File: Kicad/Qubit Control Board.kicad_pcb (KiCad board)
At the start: 6 copper layers, 144 x 81.5 mm, 147 parts, among them J1 USB_C_Receptacle_PowerOnly_6P, J2 CLK_Pins, J3 Idata, J4 Qdata, J5 SPIdata, J6 SMA, U1 LT3045xMSE, U2 TRF372017IRGZR, U3 LT3045xMSE, U4 LT3045xMSE, U5 SN65LVDS1DBV, U6 AD9743BCPZ, Y1 SiT8008xx-3x-xxN, Y2 CVHD-950-100.000

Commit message: board resizing
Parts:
- moved U2 74.1 mm to (155.8, 72.8)
- moved Y2 9.86 mm to (81.7, 30.1)
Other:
- board size 144 x 81.5 mm -> 64 x 81.5 mm

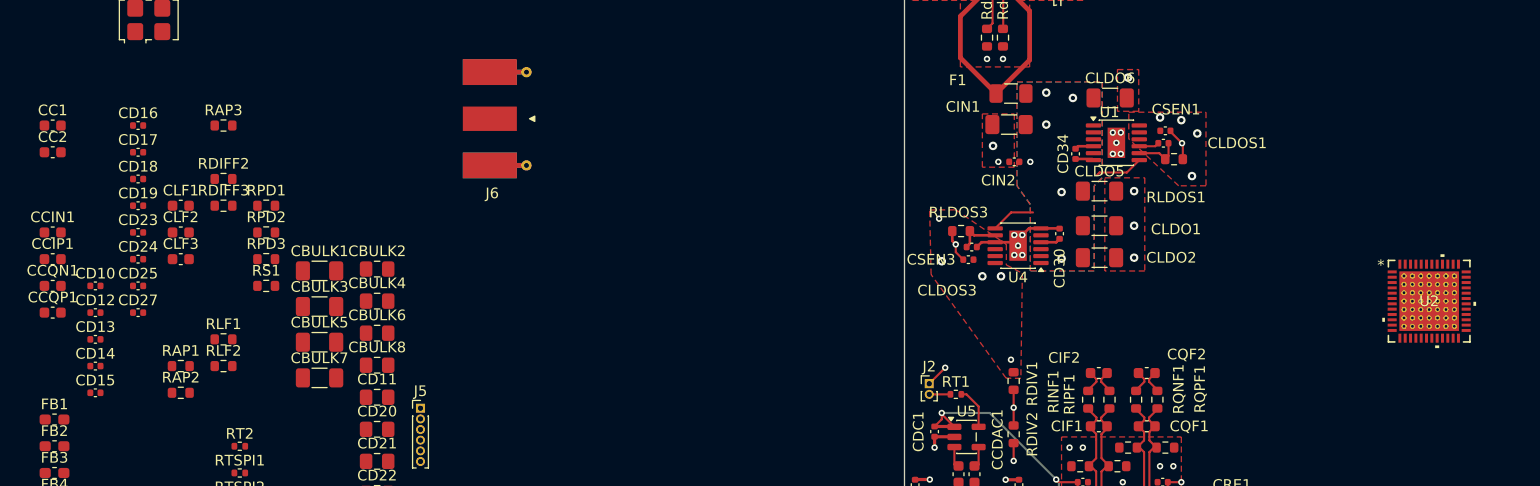
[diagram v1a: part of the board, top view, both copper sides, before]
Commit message: Added bulk caps to 3.3 and 1.8 (routing)
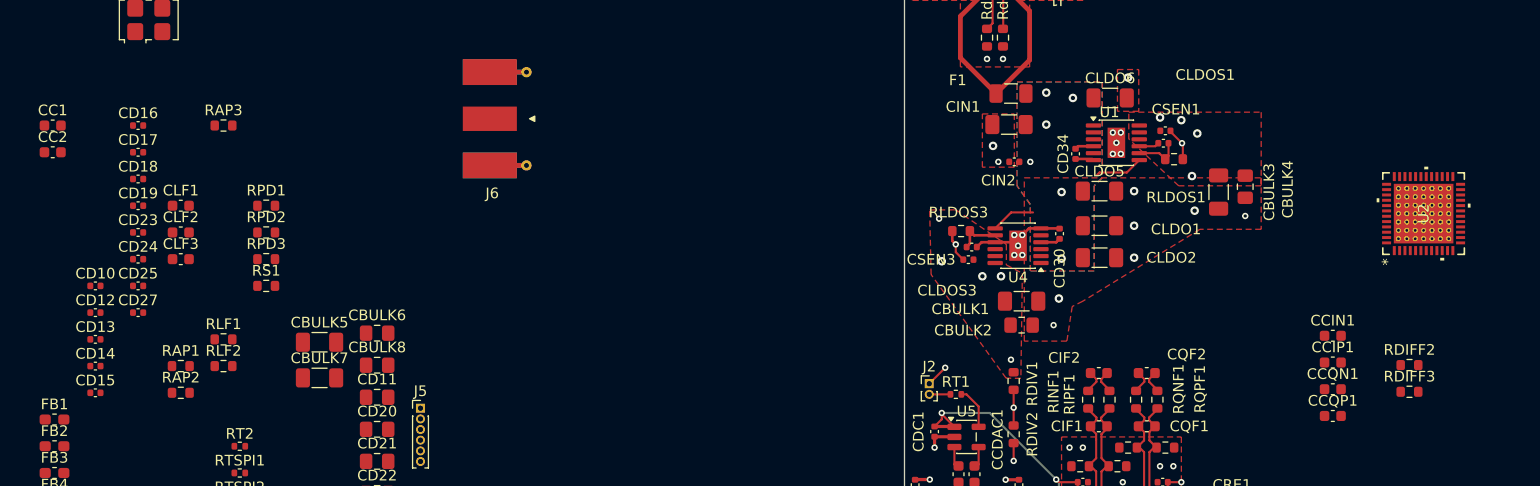
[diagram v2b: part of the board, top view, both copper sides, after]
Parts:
- moved CCIN1 120.6 mm to (146.7, 76.0)
- moved CCIP1 120.6 mm to (146.7, 78.5)
- moved CCQN1 120.6 mm to (146.7, 81.0)
- moved CCQP1 120.6 mm to (146.7, 83.5)
- moved RDIFF2 112.7 mm to (153.9, 78.8)
- moved RDIFF3 112.7 mm to (153.9, 81.3)
- moved CBULK3 85.1 mm to (136.0, 62.5), turned to -90 degrees
- moved CBULK4 82.2 mm to (138.5, 62.0), turned to -90 degrees
- moved CBULK1 66.0 mm to (117.5, 72.8)
- moved CBULK2 60.8 mm to (117.5, 75.0)
- moved U2 8.24 mm to (155.2, 64.5), turned to 90 degrees
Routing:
- net GND: vias 55 -> 59

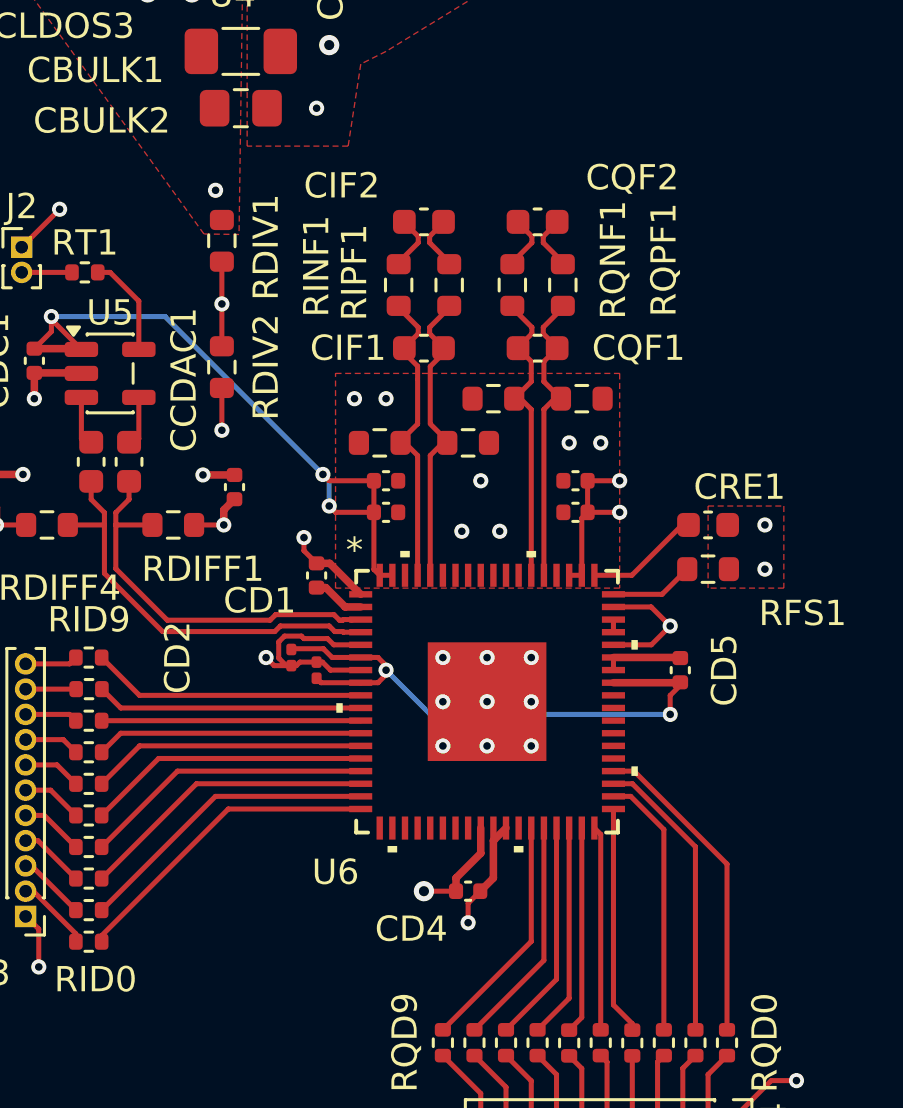
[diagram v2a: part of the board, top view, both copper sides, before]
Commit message: moved decoupling caps to the bottom
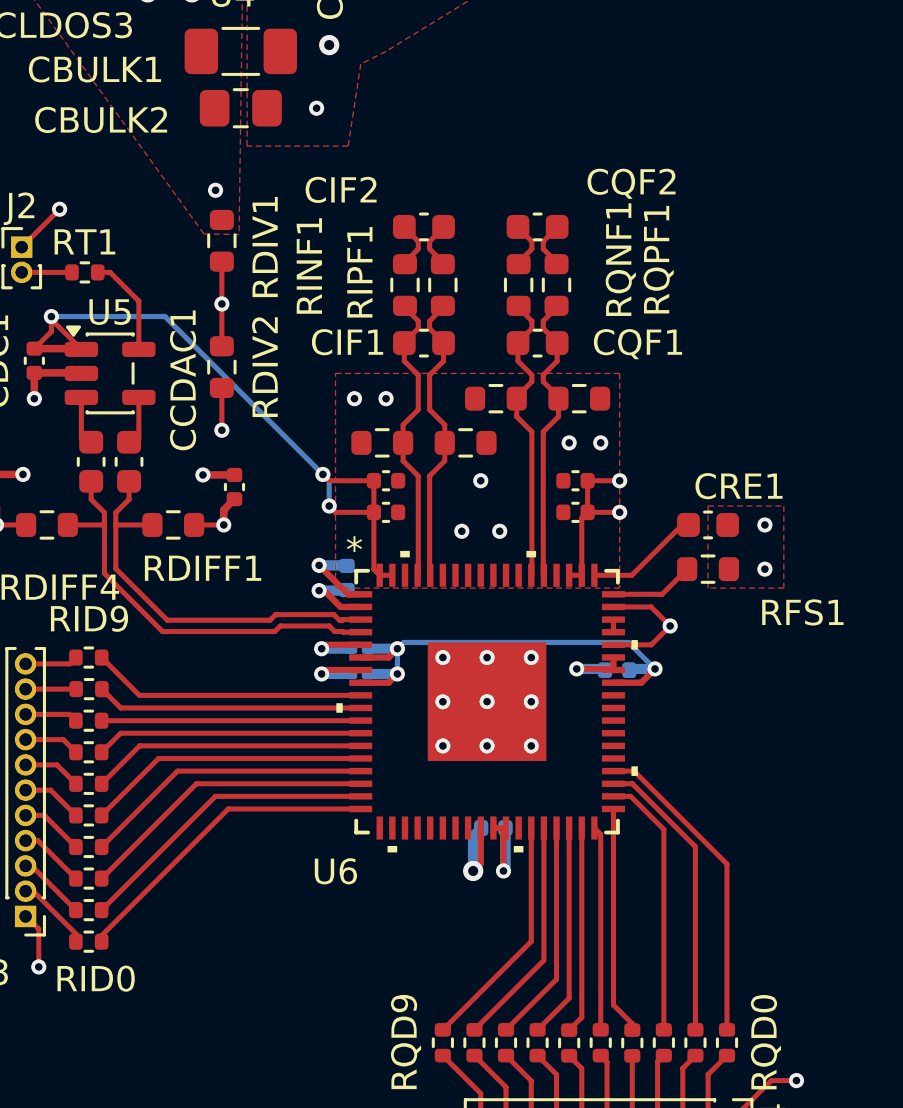
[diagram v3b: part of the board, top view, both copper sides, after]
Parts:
- CD1, CD2, CD3, CD4, CD5: moved to B.Cu
- moved CD2 2.72 mm to (122.2, 96.4), turned to 0 degrees
- moved CD4 2.69 mm to (127.5, 103.5)
- moved CD5 2.50 mm to (132.4, 97.2), turned to 180 degrees
- moved CD3 1.71 mm to (122.2, 97.4), turned to 0 degrees
- moved CD1 1.20 mm to (121.7, 93.6)
- moved RINF1 0.25 mm to (125.5, 82.0)
- moved RIPF1 0.25 mm to (124.0, 82.0)
- moved RQNF1 0.25 mm to (128.5, 82.0)
- moved RQPF1 0.25 mm to (130.0, 82.0)
- moved CIF1 0.20 mm to (124.8, 84.3)
- moved CIF2 0.20 mm to (124.8, 79.7)
- moved CQF1 0.20 mm to (129.2, 84.3)
- moved CQF2 0.20 mm to (129.2, 79.7)
- moved RLOAD1 0.10 mm to (123.1, 88.2)
- moved RLOAD2 0.10 mm to (126.4, 88.2)
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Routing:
- net +1.8V: track 27.1 -> 23.6 mm, vias 8 -> 9
- net GND: track 56.0 -> 53.4 mm, vias 59 -> 62
- net +3.3V-A: track 44.4 -> 43.9 mm

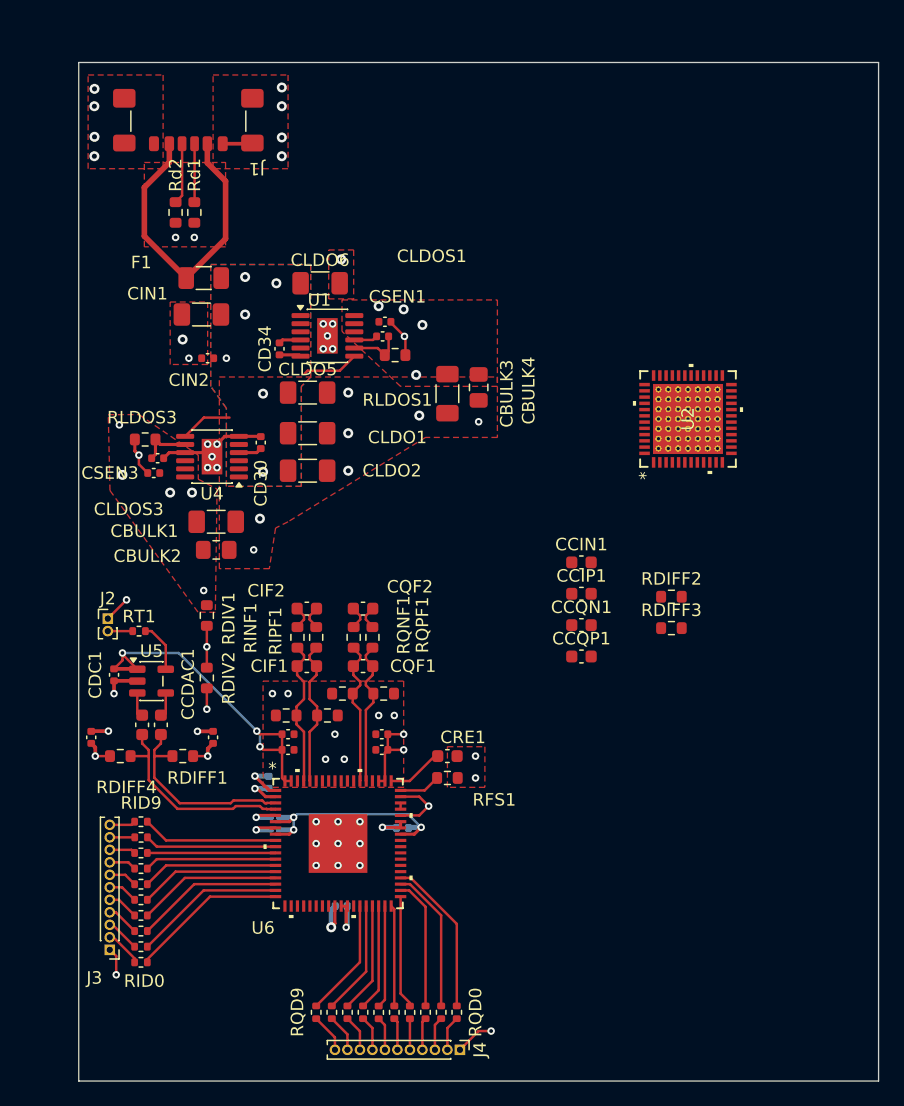
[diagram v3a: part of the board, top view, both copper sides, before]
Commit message: re doing 1.8V and 3.3V LDOs for DAC
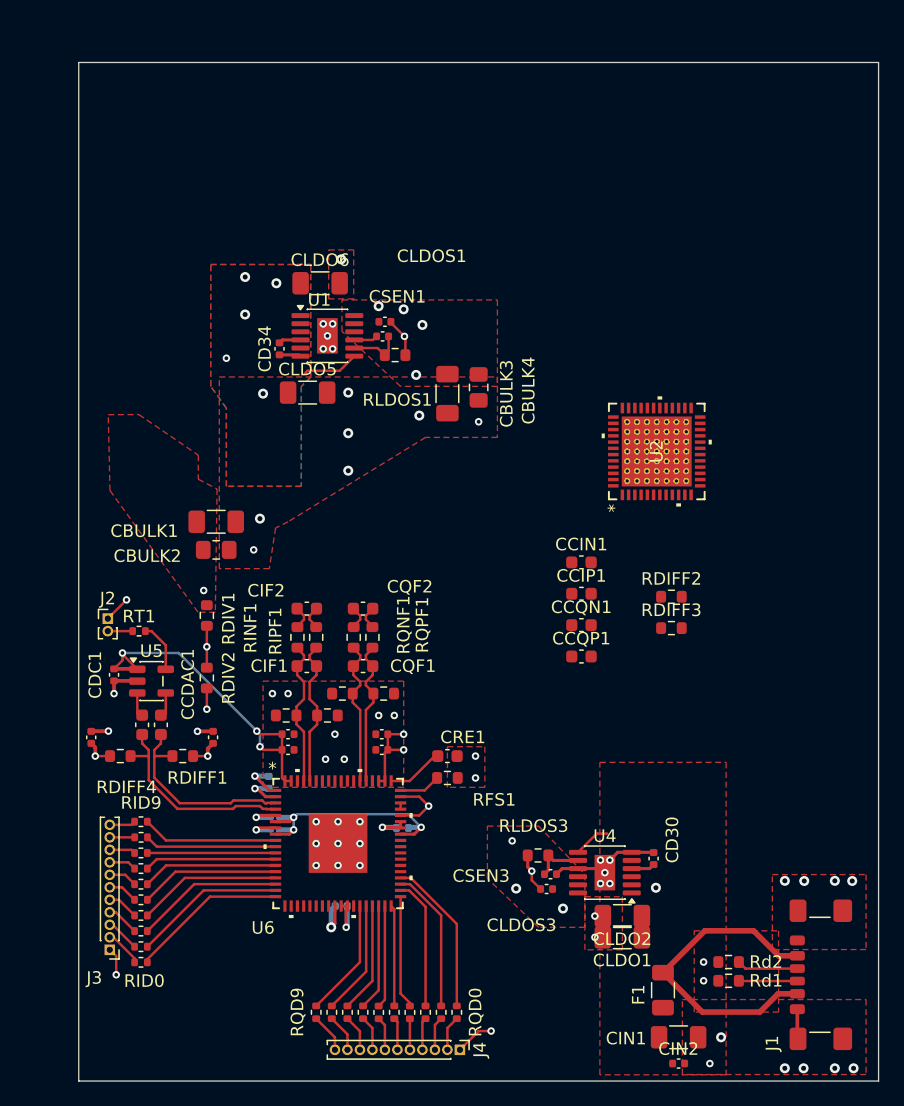
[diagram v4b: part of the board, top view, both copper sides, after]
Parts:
- moved J1 86.7 mm to (167.0, 109.0), turned to 90 degrees
- moved Rd1 74.9 mm to (158.5, 109.5), turned to 180 degrees
- moved Rd2 74.5 mm to (158.5, 108.0), turned to 180 degrees
- moved CIN1 69.3 mm to (154.5, 114.0), turned to 0 degrees
- moved CIN2 67.9 mm to (154.5, 116.1), turned to 0 degrees
- moved F1 67.8 mm to (153.2, 110.2), turned to -90 degrees
- moved CLDO1 47.6 mm to (150.0, 106.0), turned to 180 degrees
- moved CSEN3 45.8 mm to (143.9, 102.1)
- moved CD30 45.8 mm to (152.5, 99.7)
- moved CLDOS3 45.8 mm to (144.2, 101.0)
- moved RLDOS3 45.8 mm to (143.2, 99.5)
- moved U4 45.8 mm to (148.6, 100.8)
- moved CLDO2 43.6 mm to (150.0, 104.3), turned to 180 degrees
- moved U2 3.61 mm to (152.8, 67.1)
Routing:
- net +5V: track 12.4 -> 11.2 mm
- net GND: track 53.4 -> 52.7 mm, vias 62 -> 64
- net +1.8V: vias 9 -> 8

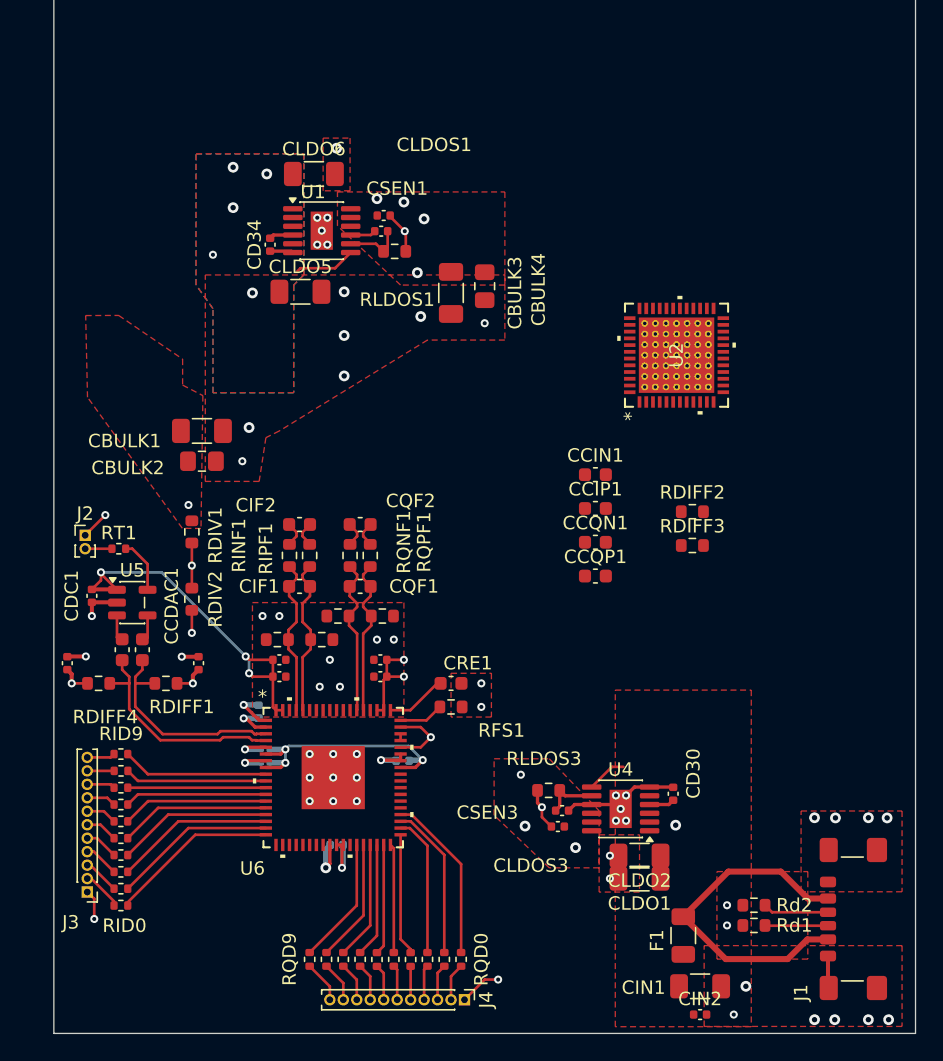
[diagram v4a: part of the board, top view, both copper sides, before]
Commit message: Finshed 1.8/3.3V LDO redo
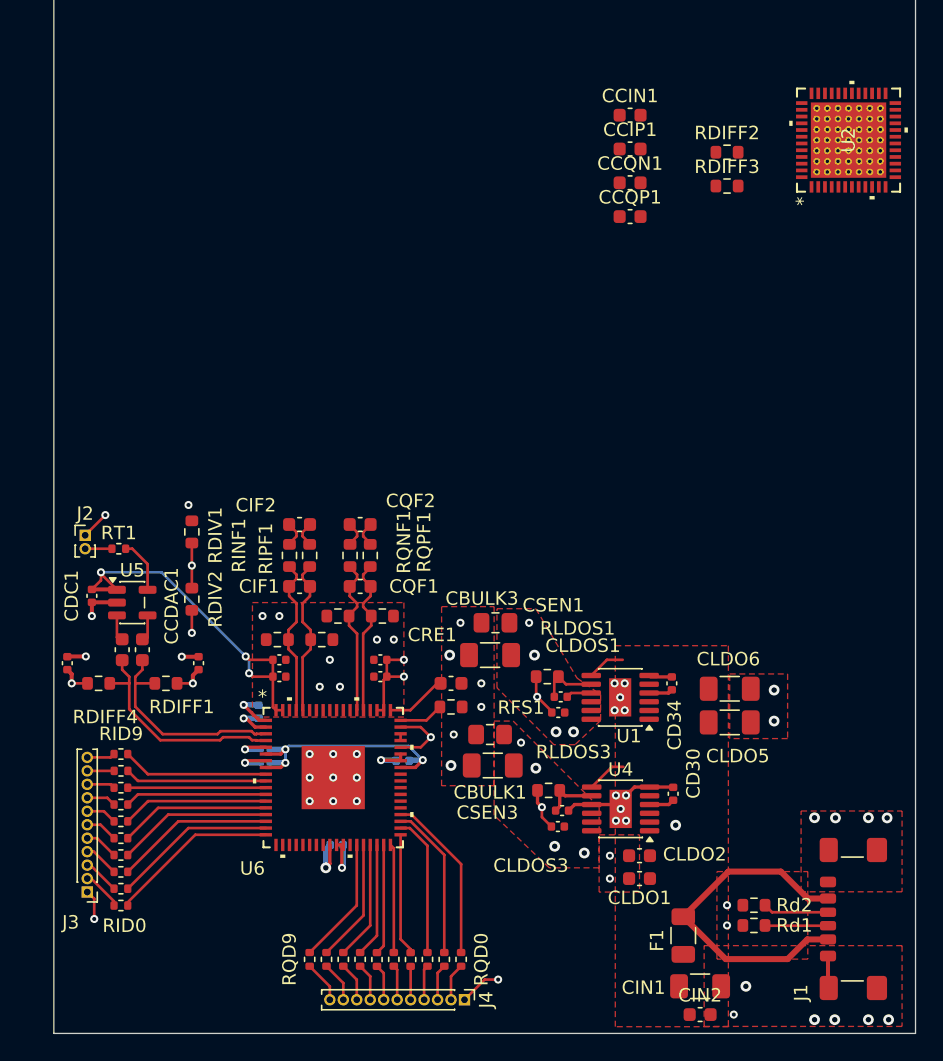
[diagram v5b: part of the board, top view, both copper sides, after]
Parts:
- CIN2: footprint Capacitor_SMD:C_0402_1005Metric -> Capacitor_SMD:C_0603_1608Metric
- CLDO1, CLDO2: footprint Capacitor_SMD:C_1206_3216Metric_Pad1.33x1.80mm_HandSolder -> Capacitor_SMD:C_0603_1608Metric
- moved CLDO6 49.2 mm to (156.7, 91.9)
- moved CLDO5 45.2 mm to (156.7, 94.4)
- moved CD34 44.2 mm to (152.4, 91.5), turned to -90 degrees
- moved U1 41.1 mm to (148.6, 92.5), turned to 180 degrees
- moved CSEN1 39.1 mm to (144.0, 93.7), turned to 0 degrees
- moved CLDOS1 37.1 mm to (144.2, 92.5), turned to 180 degrees
- moved RLDOS1 33.6 mm to (143.2, 91.0), turned to 0 degrees
- moved CBULK1 32.9 mm to (139.1, 97.6), turned to 180 degrees
- moved CBULK2 29.5 mm to (138.9, 95.3), turned to 180 degrees
- moved CBULK3 27.1 mm to (138.9, 89.4), turned to 180 degrees
- moved CCIN1 26.8 mm to (149.3, 49.3)
- moved CCIP1 26.8 mm to (149.3, 51.8)
- moved CCQP1 26.8 mm to (149.3, 56.8)
- moved CCQN1 26.8 mm to (149.3, 54.3)
- moved RDIFF2 26.8 mm to (156.5, 52.0)
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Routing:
- net +5V: track 11.2 -> 9.45 mm, vias 6 -> 1
- net GND: vias 64 -> 62
- net +1.8V: vias 8 -> 9
- removed copper zone on B.Cu, net +5V
